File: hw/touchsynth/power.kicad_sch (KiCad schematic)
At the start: 40 parts, among them J1 PWR 9-12V, U1 78L05, U2 TL072

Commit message: Schematic v2: hand-drawn sheet layouts with wires; MIDI in DNP
- draw.py/gen_sch2.py/layouts.py: placement + wiring per block, automatic
  labels for remaining split nets, short detection, junctions, KiCad
  endpoint-only connection semantics
- all 7 sheets laid out (ladder drawn as a transistor stack, diff amps,
  integrator with reset, R-2R DAC, ...); ERC 0 violations, netlist == design,
  145 simulated elements match
- MIDI input parts marked DNP (footprints kept)
- docs/touchsynth_schematic.pdf

Co-Authored-By: Claude Opus 5.5 (1M context) <noreply@anthropic.com>
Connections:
- net VIN: no longer names the net of D1.2 (A), J1.1 (Pin_1)
- net VREF_DIV: no longer names the net of C5.1, R1.2, R2.1, U2.3 (+)
- net VREF_SN: no longer names the net of C7.1, R3.2
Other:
- note added: "Ladder bias chain (from V+; VB0...VB4 = 2.4...6.4 V at V+ = 8.6 V)"
- note added: "References: VREF 4.5 V (buffered), VBIAS 1.5 V, V25 2.5 V"
- note removed: "Ladder bias chain"
- note removed: "References: VREF 4.5 V, VBIAS 1.5 V, V25 2.5 V"

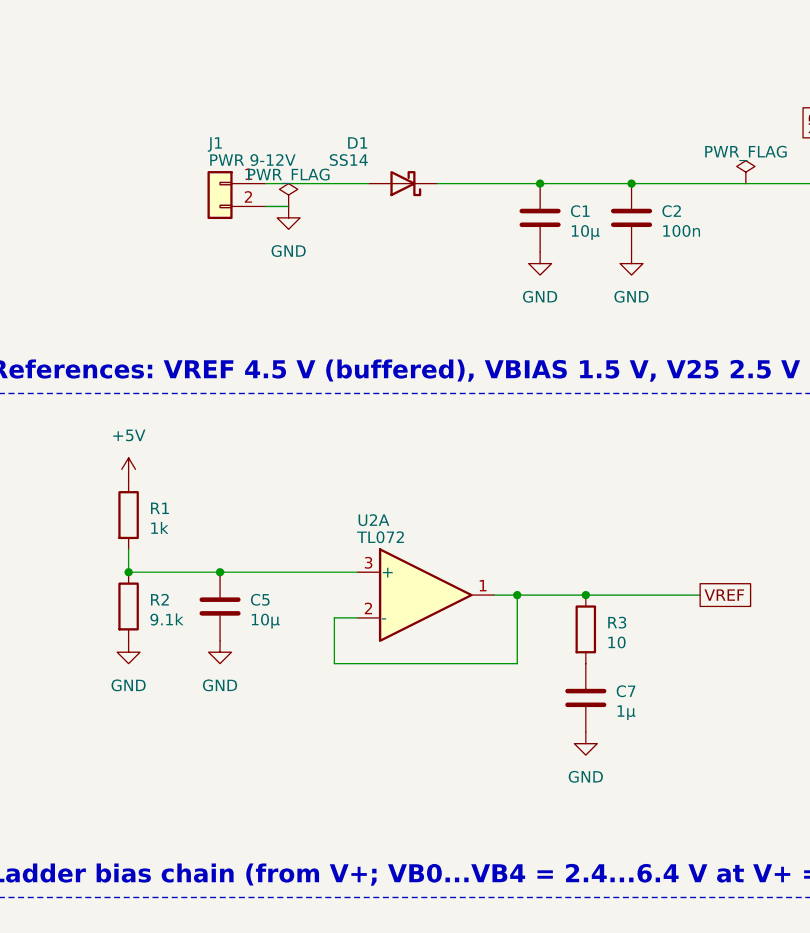
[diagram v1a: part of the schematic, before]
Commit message: PCB placement by functional block, silkscreen art, discrete LED resistors
- gen_pcb.py / pcb_place.py: 100 x 100 mm 2-layer board; keys, LEDs, connectors and test points fixed,
  ICs anchored per block, remaining parts placed greedily by connectivity inside their block
- blocks tile the circuit area with a 0.35 mm street for the dashed silkscreen frames and a reserved
  title tab each (pcb_art.py); piano keybed with hatched black keys; logo, resonant saw and ladder
  response curves on the front; signal-flow diagram on the back
- LED resistor arrays replaced by 16 discrete 4.7k 0603 (basic part) next to each LED
- deterministic schematic UUIDs, net name labels for PCB parity, op-amp re-pairing, fab.py

Co-Authored-By: Claude Opus 5.5 (1M context) <noreply@anthropic.com>
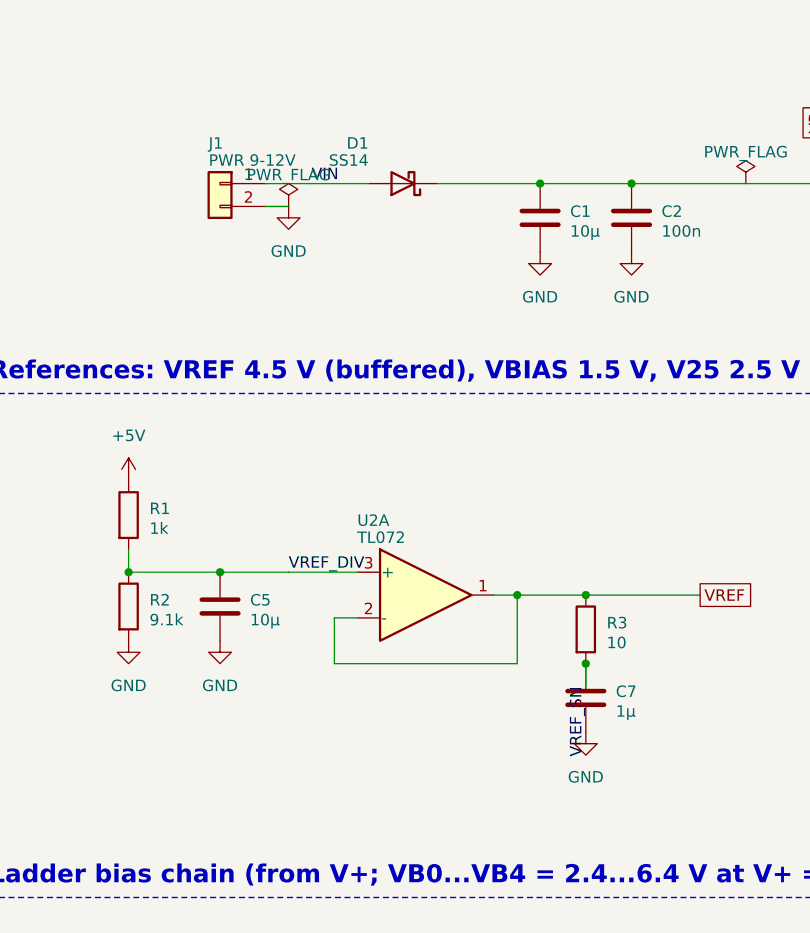
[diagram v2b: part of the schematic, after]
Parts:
- U2: Sim XVREF/XRDIF -> XVREF/XDCO
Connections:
- net VREF_DIV: now reaches C5.1, R1.2, R2.1, U2.3 (+)
- net VIN: now reaches D1.2 (A), J1.1 (Pin_1)
- net VREF_SN: now reaches C7.1, R3.2

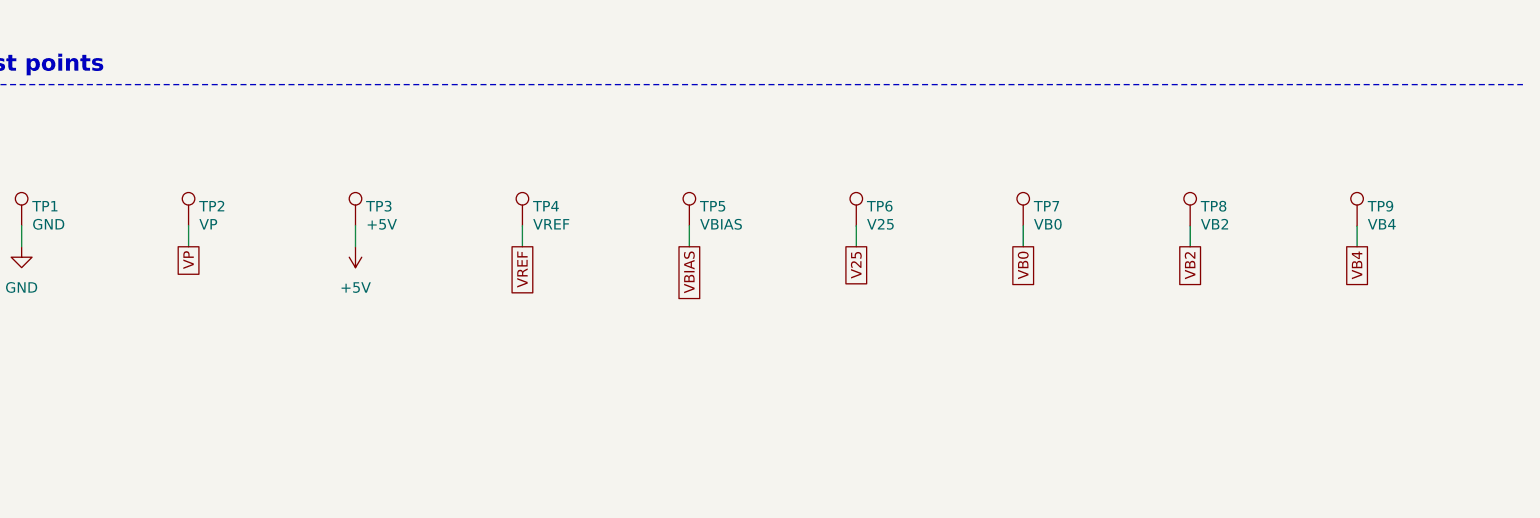
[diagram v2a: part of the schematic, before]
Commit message: 4-layer PCB: keys I/O row, trim DAC by the VCA, full routing and fab outputs
- 4 layers: F.Cu signals, In1 solid GND, In2 split power (VP analog / +5V digital / GND under the keys),
  B.Cu signals; no plane and no foreign tracks under the touch pads
- floorplan: analog blocks 72 x 36 mm in signal-flow order, right column MIDI / trim DAC / MCU,
  keys I/O row (touch muxes, LED shift registers) directly above the keys; shorter white keys,
  function pads flush with the keybed; test points inside their blocks, two THT scope-ground pins
- routing pipeline: plane stitch vias, pre-routed plane nets, Freerouting, GND via grid, island
  check, A* maze router for leftovers (pcb_maze.py), rip-up repair mode
- DRC: 0 violations, 0 unconnected, schematic parity OK; JLCPCB gerbers / BOM / CPL via fab.py
- silkscreen: back-side credits (design: cpldcpu & Claude Opus 5.5), vias kept out of the art

Co-Authored-By: Claude Opus 5.5 (1M context) <noreply@anthropic.com>
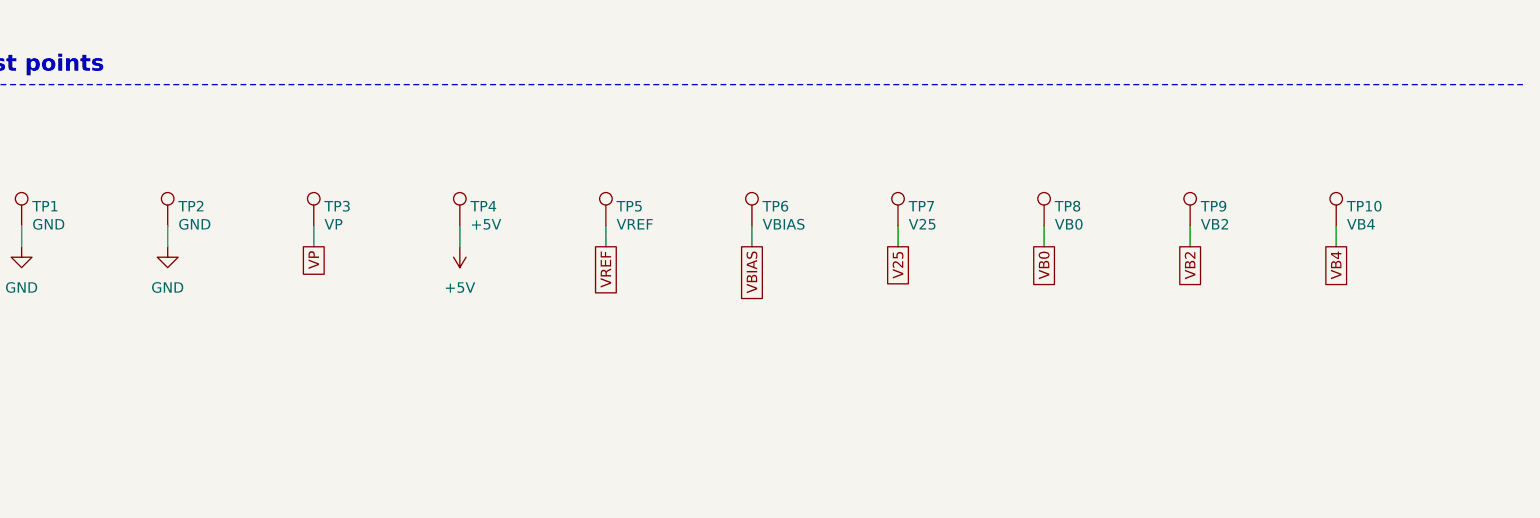
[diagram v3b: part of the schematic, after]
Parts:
- added TP10: VB4, TestPoint:TestPoint_Pad_D1.0mm, symbol Connector:TestPoint
- TP1: footprint TestPoint:TestPoint_Pad_D1.0mm -> Connector_PinHeader_2.54mm:PinHeader_1x01_P2.54mm_Vertical; Note (none) -> scope ground left
- TP2: value VP -> GND; footprint TestPoint:TestPoint_Pad_D1.0mm -> Connector_PinHeader_2.54mm:PinHeader_1x01_P2.54mm_Vertical; Note (none) -> scope ground right
- TP3: value +5V -> VP
- TP4: value VREF -> +5V
- TP5: value VBIAS -> VREF
- TP6: value V25 -> VBIAS
- TP7: value VB0 -> V25
- TP8: value VB2 -> VB0
- TP9: value VB4 -> VB2
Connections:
- net +5V: now also TP4.1; no longer TP3.1
- net GND: now also TP2.1
- net V25: now also TP7.1; no longer TP6.1
- net VB0: now also TP8.1; no longer TP7.1
- net VB2: now also TP9.1; no longer TP8.1
- net VB4: now also TP10.1; no longer TP9.1
- net VBIAS: now also TP6.1; no longer TP5.1
- net VP: now also TP3.1; no longer TP2.1
- net VREF: now also TP5.1; no longer TP4.1
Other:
- moved on the sheet: TP2, TP3, TP4, TP5, TP6, TP7, TP8, TP9
